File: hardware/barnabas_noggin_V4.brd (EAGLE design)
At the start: 100 x 80 mm, 45 parts, among them IC2 LM1117IMPX-5.0, IC3 ATMEGA328P-32MUR, J1 POWER_JACKPTH, J3 USB-mini-90 -SMD, J4 ICSP, SW1 157SW, Y1 16MHZ, Y2 12MHz

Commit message: Updated V4 schematics.
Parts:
- removed F1: FUSE_6V, barnabas_noggin_V4:FUSE_0603
- removed U$1: CH340G, barnabas_noggin_V4:SOIC16
- added F2: FUSE_6V, barnabas_noggin_V4:FUSE_0603
- added IC1: CH340G, barnabas_noggin_V4:SOIC16
- added JP7: 2.54mm, barnabas_noggin_V4:1X06
- added M1, M2, M3, M4: MOUNT_HOLE, barnabas_noggin_V4:MOUNT_HOLE
- added R7, R8, R9: 1K, barnabas_noggin_V4:R0603
- added SW2: 157SW, barnabas_noggin_V4:SWITCHES_SMD_157SW
- added U1: L9110S_DRIVER, barnabas_noggin_V4:L9110S_DRIVER
- R4: device barnabas_noggin_V4:RESISTOR_1206 -> barnabas_noggin_V4:R0603
- moved C14 355.2 mm to (14.5, 27.5), turned to 90 degrees
- moved C13 348.0 mm to (11.0, 27.5), turned to 90 degrees
- moved C12 338.3 mm to (11.0, 23.6), turned to 270 degrees
- moved C11 333.5 mm to (14.5, 23.6), turned to 270 degrees
- moved JP4 314.8 mm to (31.0, 58.3), turned to 180 degrees
- moved JP3 305.9 mm to (52.9, 58.3), turned to 180 degrees
- moved JP6 292.9 mm to (39.1, 9.90)
- moved JP5 283.4 mm to (55.1, 9.90), turned to 180 degrees
- moved JP2 256.2 mm to (64.4, 41.1), turned to 90 degrees
- moved JP1 248.7 mm to (64.3, 50.8), turned to 90 degrees
- moved SG1 206.5 mm to (62.4, 20.1)
- moved R6 202.4 mm to (61.9, 29.9)
- moved U$14 180.0 mm to (49.4, 19.6)
- moved R5 172.5 mm to (49.3, 26.5), turned to 180 degrees
- moved C10 148.6 mm to (28.8, 10.1)
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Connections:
- removed net COM: C4.2, U$1.1
- removed net N$11: L.A, R4.4
- removed net N$15: F1.1, J3.5
- new net 5V_PIN: C11.1, C12.1, C13.1, C14.1, C3.1, C5.1, C7.1, F2.2, IC1.16, IC3.18, IC3.4, IC3.6, J4.2, JP1.3, JP1.4, JP2.3, JP2.4, JP6.4, R1.2, R7.2, R8.2, R9.2
- new net N$10: L.A, R4.1
- net 3V3: now also IC1.4; no longer U$1.4
- net 5V: now also F2.1; no longer C11.1, C12.1, C13.1, C14.1, C3.1, C5.1, C7.1, IC3.18, IC3.4, IC3.6, J4.2, JP1.3, JP1.4, JP2.3, JP2.4, JP6.4, R1.2, R4.7, R4.8, U$1.16
- net D12/MISO: now also JP7.1
- net D13/SCK: now also R4.2; no longer R4.5
- net D2: now also SW2.1
- net GND: now also C4.2, IC1.1, SW2.2
- net N$12: now also IC1.8; no longer U$1.8
- net N$13: now also IC1.5; no longer U$1.5
- net N$14: now also IC1.6; no longer U$1.6
- net N$3: now also R7.1; no longer R4.3
- net N$4: now also IC1.13; no longer U$1.13
- net N$5: now also IC1.7; no longer U$1.7
- net N$6: now also IC1.2; no longer U$1.2
- net N$7: now also R8.1; no longer R4.1
- net N$8: now also IC1.3; no longer U$1.3
- net N$9: now also R9.1; no longer R4.2
- net VOUT: no longer R4.6
- net VUSB: now also J3.5; no longer F1.2
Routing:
- net RX: track 0.00 -> 40.6 mm
- net TX: track 0.00 -> 37.5 mm
- net D2: track 0.00 -> 34.2 mm
- net D3: track 0.00 -> 31.3 mm
- net D4: track 0.00 -> 29.0 mm
- net D5: track 0.00 -> 28.8 mm
- net D6: track 0.00 -> 28.0 mm
- net D7: track 0.00 -> 26.1 mm
- net 5V_PIN: track 0.00 -> 25.2 mm
- net D8: track 0.00 -> 23.1 mm
- net AREF: track 0.00 -> 22.8 mm
- net D9: track 0.00 -> 21.7 mm
- net D10: track 0.00 -> 21.4 mm
- net D13/SCK: track 0.00 -> 21.1 mm
- net D11/MOSI: track 0.00 -> 21.0 mm
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- added copper zone on layer 1, net GND
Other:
- outline, holes or cut-outs redrawn
- board text added: "BARNABAS"

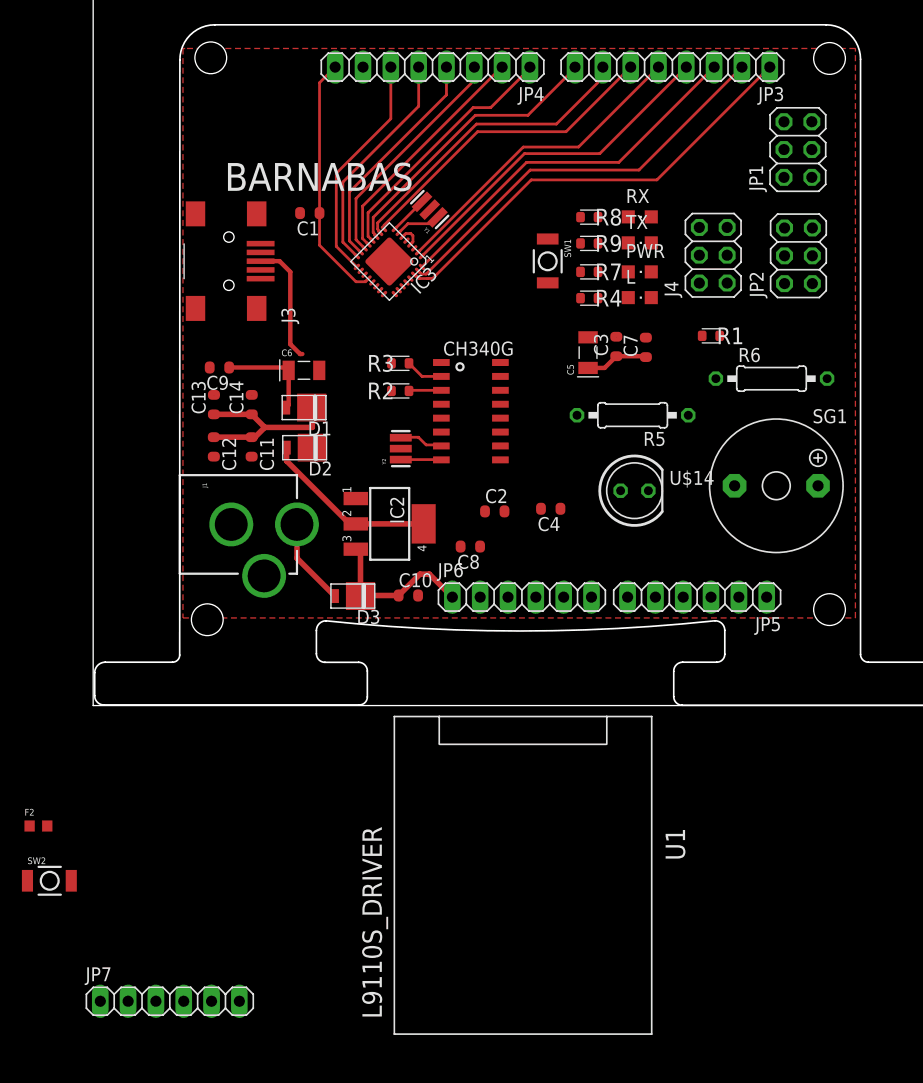
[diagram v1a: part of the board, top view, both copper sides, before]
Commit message: Added 3.3V regulator.
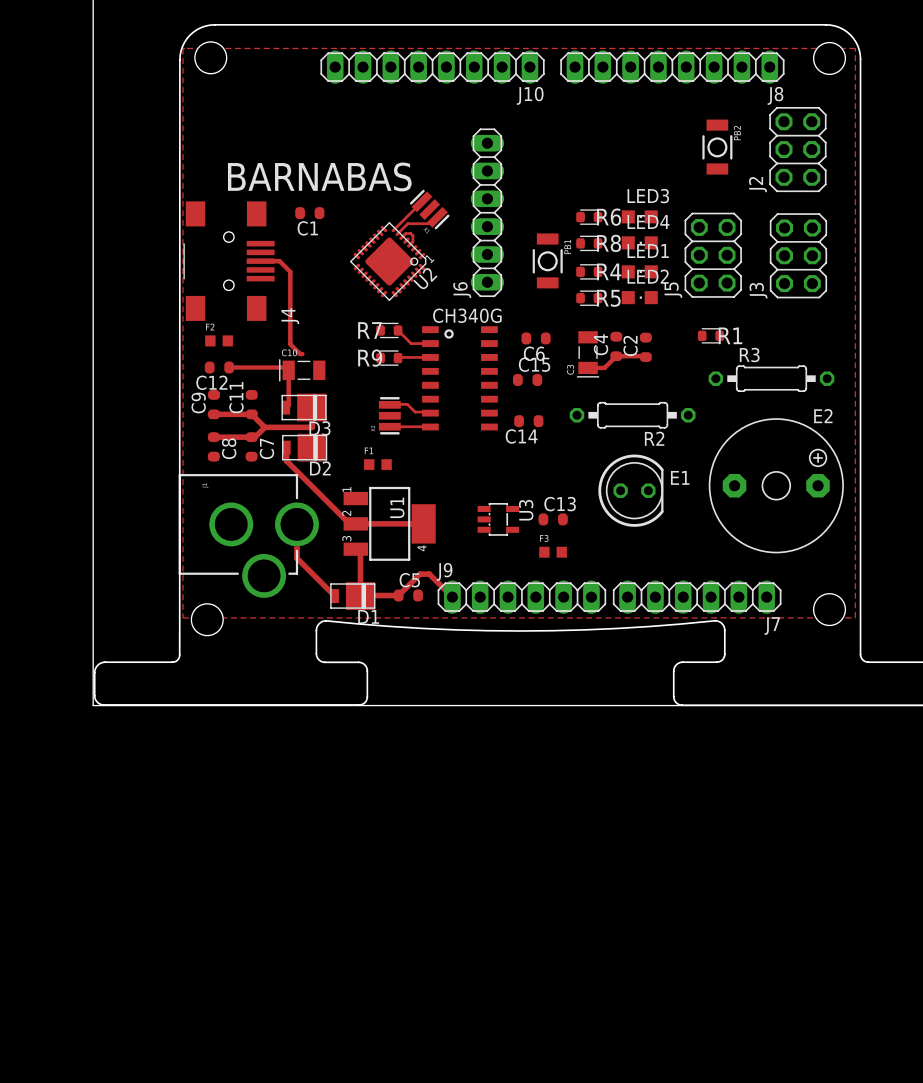
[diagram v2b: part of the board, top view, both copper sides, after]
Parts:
- removed IC1: CH340G, barnabas_noggin_V4:SOIC16
- removed IC2: LM1117IMPX-5.0, barnabas_noggin_V4:LM1117_SOT223
- removed JP2: (no value), barnabas_noggin_V4:CONNECTOR_2X3
- removed JP7: 2.54mm, barnabas_noggin_V4:1X06
- removed SW2: 157SW, barnabas_noggin_V4:SWITCHES_SMD_157SW
- removed Y2: 12MHz, barnabas_noggin_V4:CRYSTAL
- added C15: 100nF, barnabas_noggin_V4:C0603-ROUND
- added F1, F3: FUSE_6V, barnabas_noggin_V4:FUSE_0603
- added J5: ICSP, barnabas_noggin_V4:CONNECTOR_2X3
- added J6: 2.54mm, barnabas_noggin_V4:1X06
- added PB2: 157SW, barnabas_noggin_V4:SWITCHES_SMD_157SW
- added U3: LP2985-XXDBVR, barnabas_noggin_V4:SOT23-DBV
- added U4: CH340G, barnabas_noggin_V4:SOIC16
- added U5: L9110S_DRIVER, barnabas_noggin_V4:L9110S_DRIVER
- added X2: 12MHz, barnabas_noggin_V4:CRYSTAL
- C10, C3: value 1uF -> 4.7uF; device barnabas_noggin_V4:C0603-ROUND -> barnabas_noggin_V4:TAN-A
- C13, C2, C4: value 100nF -> 1uF
- C5, C6: value 4.7uF -> 1uF; device barnabas_noggin_V4:TAN-A -> barnabas_noggin_V4:C0603-ROUND
- C7, C8: value 1uF -> 100nF
- J2: value (none) -> ICSP
- J3: value USB-mini-90 -SMD -> ICSP; device barnabas_noggin_V4:CONNECTOR_USB_MINI-B -> barnabas_noggin_V4:CONNECTOR_2X3
- J4: value ICSP -> USB-mini-90 -SMD; device barnabas_noggin_V4:CONNECTOR_2X3 -> barnabas_noggin_V4:CONNECTOR_USB_MINI-B
- R2: value 1K -> 4.7K; device barnabas_noggin_V4:R0603 -> barnabas_noggin_V4:RESISTOR_PTH
- R3: value 1K -> 470; device barnabas_noggin_V4:R0603 -> barnabas_noggin_V4:RESISTOR_PTH
- R5: value 4.7K -> 1K; device barnabas_noggin_V4:RESISTOR_PTH -> barnabas_noggin_V4:R0603
- R6: value 470 -> 1K; device barnabas_noggin_V4:RESISTOR_PTH -> barnabas_noggin_V4:R0603
- U1: value L9110S_DRIVER -> LM1117IMPX-5.0; device barnabas_noggin_V4:L9110S_DRIVER -> barnabas_noggin_V4:LM1117_SOT223
- moved J3 49.2 mm to (64.4, 41.1)
- moved F2 47.3 mm to (11.5, 33.3)
- moved J4 41.4 mm to (15.3, 39.0)
- moved C7 37.1 mm to (14.5, 23.6), turned to 270 degrees
- moved R3 33.9 mm to (61.9, 29.9), turned to 0 degrees
- moved C13 32.7 mm to (42.0, 17.0), turned to 0 degrees
- moved U1 29.7 mm to (27.1, 16.6), turned to 270 degrees
- moved C5 26.5 mm to (28.8, 10.1), turned to 0 degrees
- moved C14 25.3 mm to (39.8, 26.0), turned to 180 degrees
- moved C8 25.1 mm to (11.0, 23.6), turned to 270 degrees
- moved C10 23.3 mm to (17.9, 30.6)
- moved C6 22.8 mm to (40.4, 33.5), turned to 180 degrees
- moved R6 22.2 mm to (45.3, 44.6)
- moved R2 21.3 mm to (49.3, 26.5)
- moved R9 21.0 mm to (27.0, 31.7), turned to 180 degrees
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- renumbered IC3 to U2, JP1 to J2, JP3 to J8, JP4 to J10, JP5 to J7, JP6 to J9, L to LED2, PWR to LED1, RX to LED3, SG1 to E2, SW1 to PB1, TX to LED4, U$14 to E1, Y1 to X1
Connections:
- removed net 3V3: C4.1, IC1.4, J9.5
- new net 3.3V: C13.1, F3.2, U3.5
- new net 3.3V_PIN: F3.1, J9.5
- new net N$11: C14.1, U4.4
- new net N$17: F2.1, J4.5
- net 5V: now also C11.1, C2.1, C3.1, C4.1, C7.1, C8.1, C9.1, D3.P$1, F1.1, R1.2, R4.2, R6.2, R8.2, U2.18, U2.4, U2.6, U3.1, U3.3, U4.16; no longer D1.P$1, F2.1
- net 5V_PIN: now also F1.2, J3.3, J3.4, J5.2, J6.3; no longer C11.1, C12.1, C13.1, C14.1, C3.1, C5.1, C7.1, F2.2, IC1.16, J4.2, JP2.3, JP2.4, R1.2, R7.2, R8.2, R9.2, U2.18, U2.4, U2.6
- net D10: now also J3.5, J6.2; no longer JP2.5
- net D11/MOSI: now also J3.6, J5.4, J6.5; no longer J4.4, JP2.6
- net D12/MISO: now also J5.1, J6.1; no longer J4.1, JP7.1
- net D13/SCK: now also J5.3, R5.2; no longer J4.3, R4.2
- net D2: now also PB2.1; no longer SW2.1
- net D6: now also R3.1; no longer R6.1
- net D7: now also R2.1; no longer R5.1
- net D8: now also J6.6
- net GND: now also C2.2, J3.2, J4.1, J4.7, J4.8, J4.9, J5.6, J6.4, PB2.2, U1.1, U3.2, U4.1, X2.2; no longer IC1.1, IC2.1, J3.6, J3.7, J3.8, J3.9, JP2.1, JP2.2, SW2.2, Y2.2
- net N$10: now also R5.1; no longer R4.1
- net N$12: now also U4.8, X2.1; no longer IC1.8, Y2.1
- net N$13: now also J4.3, U4.5; no longer IC1.5, J3.3
- net N$14: now also J4.4, U4.6; no longer IC1.6, J3.4
- net N$16: now also D1.P$2; no longer D3.P$2
- net N$18: now also R2.2; no longer R5.2
- net N$19: now also R3.2; no longer R6.2
- net N$3: now also R4.1; no longer R7.1
- net N$4: now also C15.1, U4.13; no longer C2.1, IC1.13
- net N$5: now also U4.7, X2.3; no longer IC1.7, Y2.3
- net N$6: now also R7.1, U4.2; no longer IC1.2, R3.1
- net N$7: now also R6.1; no longer R8.1
- net N$8: now also R9.1, U4.3; no longer IC1.3, R2.1
- net N$9: now also R8.1; no longer R9.1
- net RESET: now also C15.2, J5.5; no longer C2.2, J4.5
- net RX: now also R7.2; no longer R3.2
- net TX: now also R9.2; no longer R2.2
- net VIN: now also C5.1, D1.P$1, U1.3; no longer C10.1, D3.P$1, IC2.3
- net VOUT: now also C6.1, U1.2, U1.4; no longer C8.1, IC2.2, IC2.4
- net VUSB: now also C10.1, C12.1, D3.P$2, F2.2; no longer C6.1, C9.1, D1.P$2, J3.5
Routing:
- net RX: track 40.6 -> 0.00 mm
- net TX: track 37.5 -> 0.00 mm
- net D2: track 34.2 -> 0.00 mm
- net D3: track 31.3 -> 0.00 mm
- net D4: track 29.0 -> 0.00 mm
- net D5: track 28.8 -> 0.00 mm
- net D6: track 28.0 -> 0.00 mm
- net D7: track 26.1 -> 0.00 mm
- net 5V_PIN: track 25.2 -> 0.00 mm
- net D8: track 23.1 -> 0.00 mm
- net AREF: track 22.8 -> 0.00 mm
- net 5V: track 2.15 -> 24.1 mm
- net D9: track 21.7 -> 0.00 mm
- net D10: track 21.4 -> 0.00 mm
- net D13/SCK: track 21.1 -> 0.00 mm
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
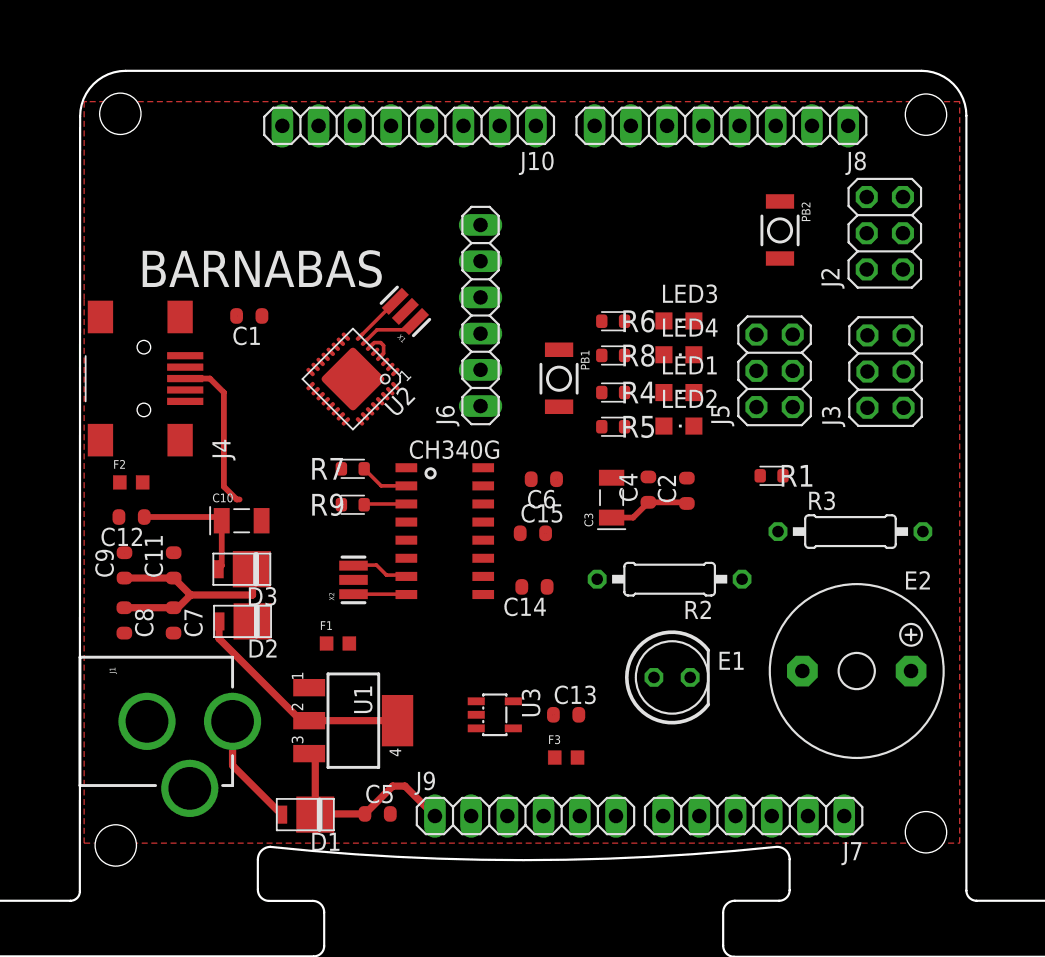
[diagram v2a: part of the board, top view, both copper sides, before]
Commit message: complete routing
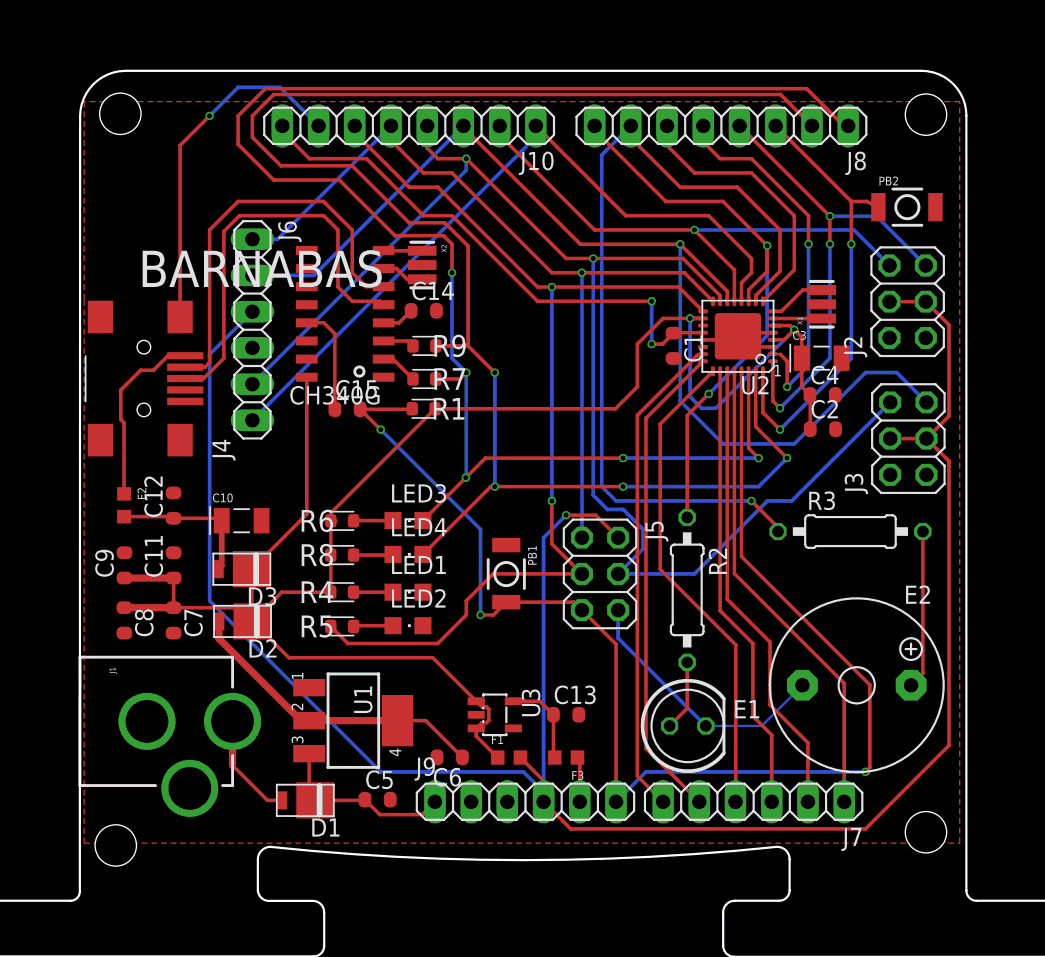
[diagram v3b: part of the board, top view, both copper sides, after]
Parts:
- moved U5 56.1 mm to (18.7, 32.3)
- moved C1 29.8 mm to (49.5, 42.9), turned to 270 degrees
- moved X1 29.2 mm to (59.9, 45.8), turned to 90 degrees
- moved U2 27.2 mm to (54.0, 43.5), turned to 180 degrees
- moved R1 24.8 mm to (32.0, 38.5)
- moved R5 23.6 mm to (26.3, 23.2), turned to 180 degrees
- moved R8 23.6 mm to (26.3, 28.2), turned to 180 degrees
- moved LED1 23.6 mm to (30.9, 25.6)
- moved LED2 23.6 mm to (30.9, 23.2)
- moved LED4 23.6 mm to (30.9, 28.2)
- moved R4 23.6 mm to (26.3, 25.6), turned to 180 degrees
- moved R6 23.6 mm to (26.3, 30.6), turned to 180 degrees
- moved LED3 23.6 mm to (30.9, 30.6)
- moved X2 22.6 mm to (31.9, 48.5), turned to 270 degrees
- moved C14 20.9 mm to (32.0, 45.3), turned to 0 degrees
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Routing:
- net 5V_PIN: track 0.00 -> 149.8 mm, vias 0 -> 1
- net TX: track 0.00 -> 115.8 mm, vias 0 -> 4
- net RX: track 0.00 -> 115.4 mm, vias 0 -> 5
- net 5V: track 24.1 -> 130.6 mm, vias 0 -> 2
- net D11/MOSI: track 0.00 -> 97.8 mm, vias 0 -> 2
- net RESET: track 0.00 -> 94.1 mm, vias 0 -> 3
- net D10: track 0.00 -> 75.7 mm, vias 0 -> 1
- net D13/SCK: track 0.00 -> 71.8 mm, vias 0 -> 2
- net D12/MISO: track 0.00 -> 60.1 mm, vias 0 -> 1
- net D6: track 0.00 -> 59.7 mm, vias 0 -> 1
- net D8: track 0.00 -> 51.2 mm
- net GND: track 0.00 -> 51.0 mm, vias 0 -> 1
- net D7: track 0.00 -> 41.6 mm, vias 0 -> 2
- net AREF: track 0.00 -> 38.6 mm, vias 0 -> 2
- net D9: track 0.00 -> 37.9 mm, vias 0 -> 1
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
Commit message: Update board surface text.
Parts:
- added U$14: (no value), barnabas_noggin_V4:BARNABAS_LOGO
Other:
- board text added: "3.3V"
- board text added: "4.7KΩ"
- board text added: "470Ω"
- board text added: "5V"
- board text added: "7V - 12V"
- board text added: "A0"
- board text added: "A1"
- board text added: "A2"
- board text added: "A3"
- board text added: "A4"
- board text added: "A5"
- board text added: "BUZZER"
- board text added: "Barnabas Noggin"
- board text added: "Build. Learn. Teach. Inspire."
- board text added: "D10"
- board text added: "D11"
- board text added: "D12"
- board text added: "D13"
- board text added: "D2"
- board text added: "D3"
- board text added: "D4"
- board text added: "D5"
- board text added: "D6"
- board text added: "D7"
- board text added: "D8"
- board text added: "D9"
- board text added: "GND"
- board text added: "LED"
- board text added: "REF"
- board text added: "RST"
- board text added: "RX"
- board text added: "Rev 2C"
- board text added: "SERVO10"
- board text added: "SERVO11"
- board text added: "SERVO3"
- board text added: "SERVO9"
- board text added: "TX"
- board text added: "VIN"
- board text added: "www.barnabasrobotics.com"
- board text removed: "BARNABAS"
